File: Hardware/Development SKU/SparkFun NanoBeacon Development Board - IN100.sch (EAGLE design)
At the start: 34 parts, among them J3 Vertical Qwiic Connector, U1 IN100, Y1 CRYSTAL-26MHZSMD-3.2X2.5

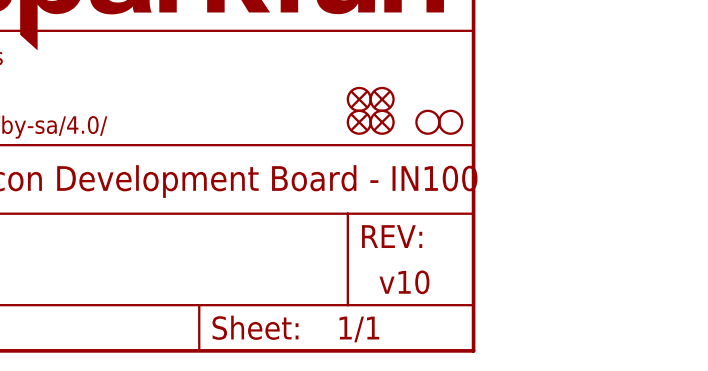
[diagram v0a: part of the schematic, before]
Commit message: v11 updates
Bump version number
Update board name in silk
Change "VBATT" silk to "Battery"
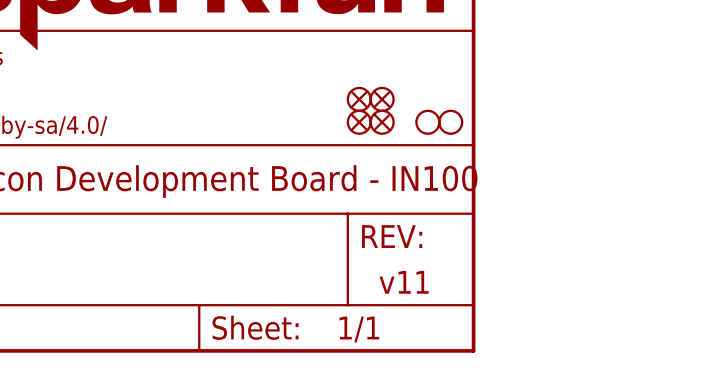
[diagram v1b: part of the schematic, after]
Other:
- note added: "v11"
- note removed: "v10"
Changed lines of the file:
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@@
 <sheet>
 <plain>
-<text x="241.3" y="7.62" size="2.54" layer="94" font="vector" align="center">v10</text>
+<text x="241.3" y="7.62" size="2.54" layer="94" font="vector" align="center">v11</text>
 <text x="175.26" y="12.7" size="2.54" layer="94" font="vector" align="center">Dryw Wade</text>
 <text x="73.66" y="63.5" size="2.54" layer="94" font="vector" align="center">Connectors</text>

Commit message: Minor updates
Nudge bottom SFE silk logo away from edge
Increase size of Qwiic logo
Nudge vias along bottom edge
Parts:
- LOGO3: value QWIIC_LOGO_3MM -> QWIIC_LOGO_5MM; device SparkFun-Aesthetics:QWIIC_LOGO_3MM -> SparkFun-Aesthetics:QWIIC_LOGO_5MM
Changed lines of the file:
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@@
 <part name="RST" library="SparkFun-Switches" deviceset="MOMENTARY-SWITCH-SPST" device="-SMD-4.6X2.8MM"/>
 <part name="GND12" library="SparkFun-PowerSymbols" deviceset="GND" device=""/>
-<part name="LOGO3" library="SparkFun-Aesthetics" deviceset="QWIIC_LOGO" device="_3MM"/>
+<part name="LOGO3" library="SparkFun-Aesthetics" deviceset="QWIIC_LOGO" device="_5MM" value="QWIIC_LOGO_5MM"/>
 <part name="PRO" library="SparkFun-Aesthetics" deviceset="PROD_ID_PASTE" device="_SILK" value="PROD_ID_PASTE_SILK"/>
 <part name="DEV" library="SparkFun-Aesthetics" deviceset="PROD_ID_PASTE" device="_SILK"/>
